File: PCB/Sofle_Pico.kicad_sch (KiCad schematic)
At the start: 83 parts, among them J2 MJ-4PP-9, Q1 Si2301CDS, SW1 SW_PUSH, SW10 SW_PUSH, SW11 SW_PUSH, SW12 SW_PUSH, SW13 SW_PUSH, SW14 SW_PUSH, SW15 SW_PUSH, SW16 SW_PUSH, SW17 SW_PUSH, SW18 SW_PUSH, SW19 SW_PUSH, SW2 SW_PUSH, SW20 SW_PUSH, SW21 SW_PUSH, SW22 SW_PUSH, SW23 SW_PUSH, SW24 SW_PUSH, SW25 SW_PUSH, SW26 SW_PUSH, SW27 SW_PUSH, SW28 SW_PUSH, SW29 SW_PUSH, SW3 SW_PUSH, SW30 SW_PUSH, SW31 SW_PUSH, SW32 SW_PUSH, SW33 SW_PUSH, SW34 SW_PUSH, SW35 SW_PUSH, SW36 SW_PUSH, SW4 SW_PUSH, SW5 SW_PUSH, SW6 SW_PUSH, SW7 SW_PUSH, SW8 SW_PUSH, SW9 SW_PUSH, U2 Pico

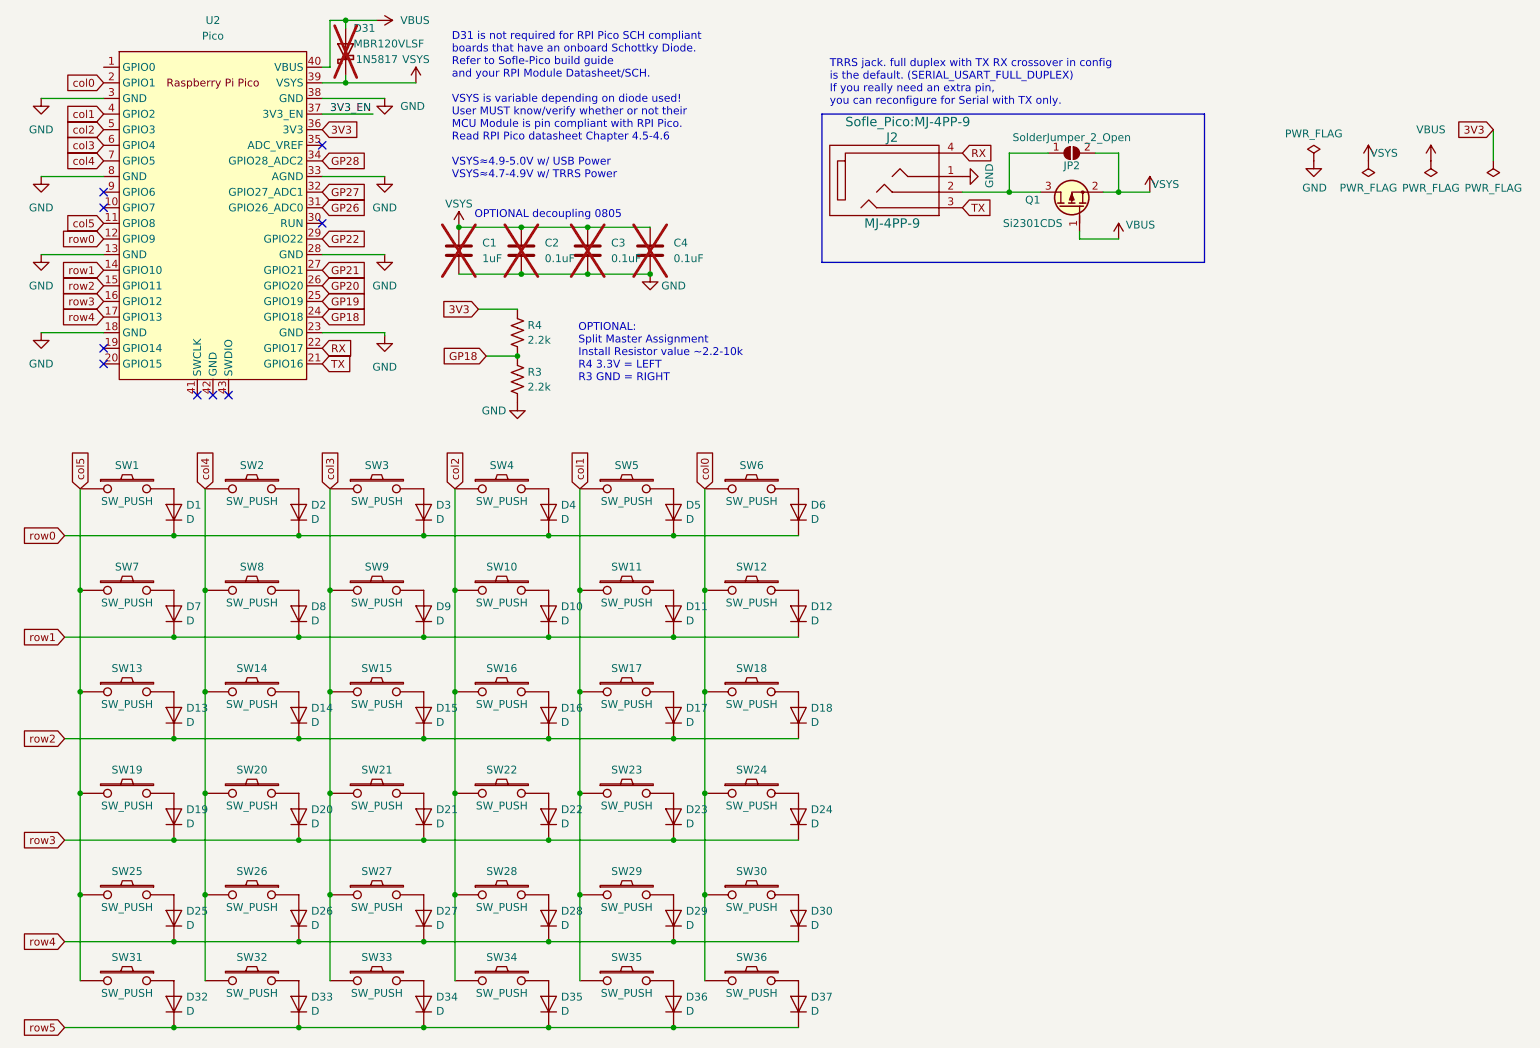
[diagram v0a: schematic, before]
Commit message: second board is not smart
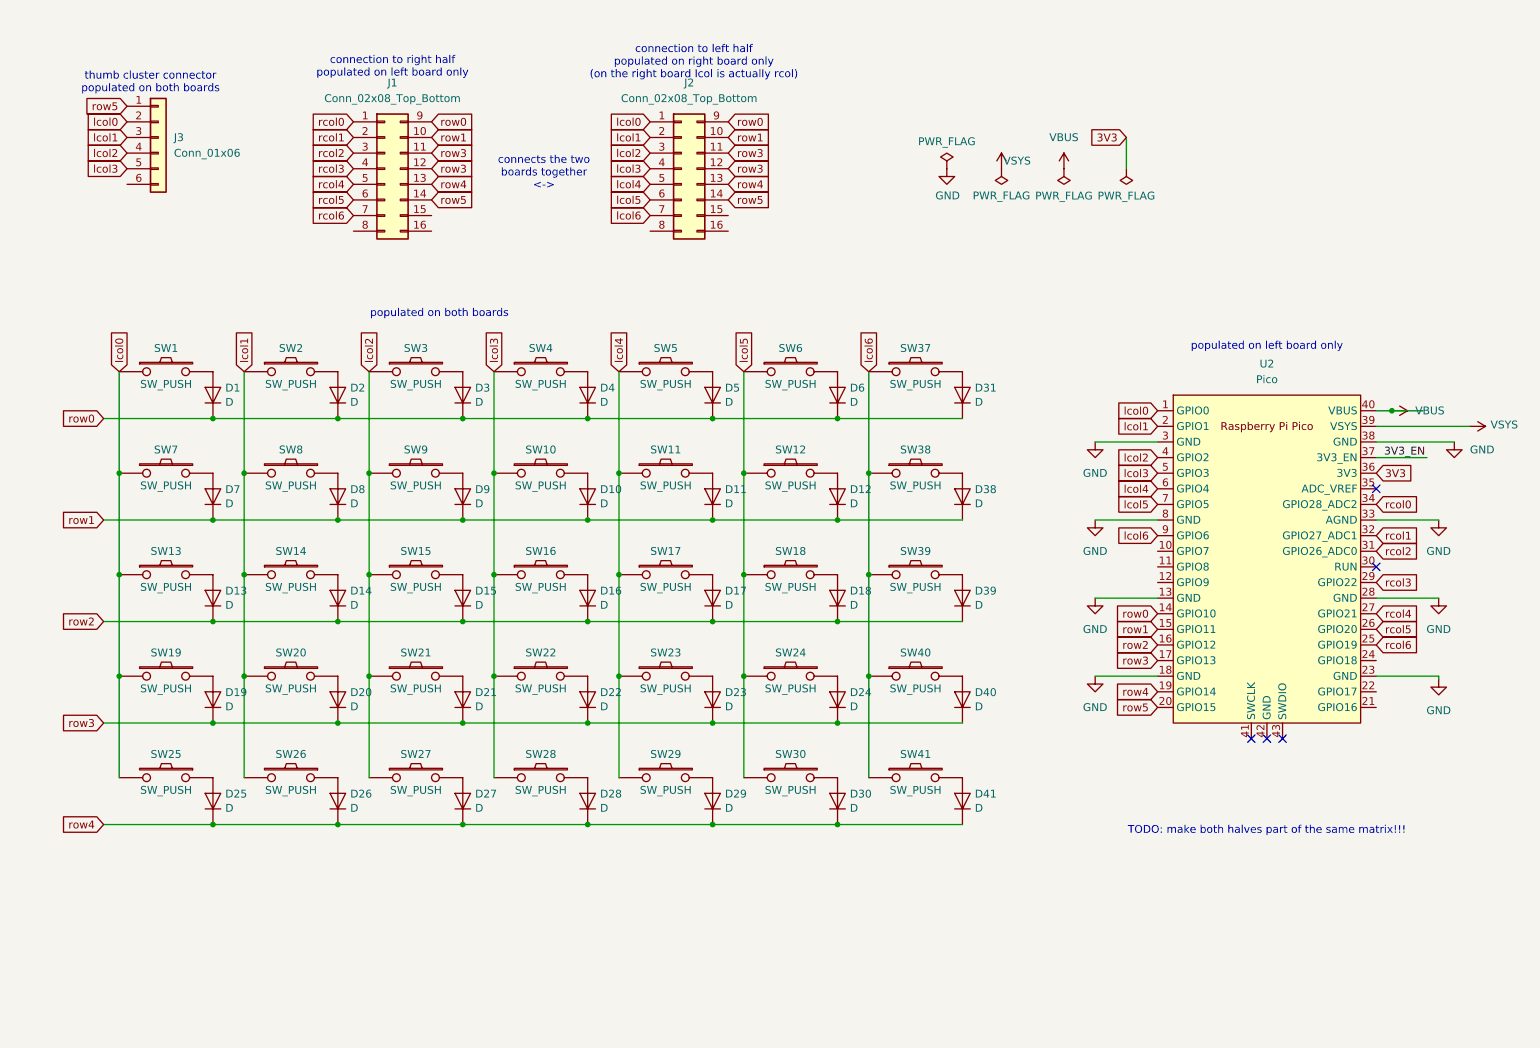
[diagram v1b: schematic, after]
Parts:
- removed C1: 1uF, Capacitor_SMD:C_0805_2012Metric_Pad1.18x1.45mm_HandSolder, symbol Device:C
- removed C2, C3, C4: 0.1uF, Capacitor_SMD:C_0805_2012Metric_Pad1.18x1.45mm_HandSolder, symbol Device:C
- removed D31: MBR120VLSF, Sofle_Pico:D_SOD-123_DO-41_7.62mm_Hybrid_DoubleSided, symbol Diode:1N5817
- removed D32, D33, D34, D35, D36, D37: D, Sofle_Pico:D_SOD-123_DO-35_Hybrid_DoubleSided_V2, symbol SofleKeyboard-rescue:D-Lily58-cache-Lily58_Pro-rescue
- removed J2: MJ-4PP-9, Sofle_Pico:MJ-4PP-9, symbol Sofle_Pico:MJ-4PP-9
- removed JP2: SolderJumper_2_Open, Sofle_Pico:Level Shifter Bypass Jumper, symbol Sofle_Pico:SolderJumper_2_Open
- removed Q1: Si2301CDS, Package_TO_SOT_SMD_AKL:SOT-23, symbol PCM_Transistor_MOSFET_AKL:DMG2305UX
- removed R3, R4: 2.2k, Sofle_Pico:Res_1206_SMD_6.3mm_TH_Hybrid, symbol Device:R_US
- removed SW31, SW32, SW33, SW34, SW35, SW36: SW_PUSH, Sofle_Pico:Cherry_MX_DS_Hotswap_v3.5.4, symbol Sofle_Pico:SW_PUSH
- added D31, D38, D39, D40, D41: D, Sofle_Pico:D_SOD-123_DO-35_Hybrid_DoubleSided_V2, symbol SofleKeyboard-rescue:D-Lily58-cache-Lily58_Pro-rescue
- added J1, J2: Conn_02x08_Top_Bottom, Connector_PinHeader_1.27mm:PinHeader_2x08_P1.27mm_Horizontal, symbol Connector_Generic:Conn_02x08_Top_Bottom
- added J3: Conn_01x06, Connector_PinHeader_1.27mm:PinHeader_1x06_P1.27mm_Horizontal, symbol Connector_Generic:Conn_01x06
- added SW37, SW38, SW39, SW40, SW41: SW_PUSH, Sofle_Pico:Cherry_MX_DS_Hotswap_v3.5.4, symbol Sofle_Pico:SW_PUSH
- U2: footprint Sofle_Pico:RPi_Pico_SMD_TH_DS -> Module:RaspberryPi_Pico_SMD_HandSolder
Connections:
- net row0: now also U2.14 (GPIO10), D31.1 (K), J1.9 (Pin_9), J2.9 (Pin_9); no longer U2.12 (GPIO9)
- net row1: now also U2.15 (GPIO11), D38.1 (K), J1.10 (Pin_10), J2.10 (Pin_10); no longer U2.14 (GPIO10)
- net row2: now also U2.16 (GPIO12), D39.1 (K); no longer U2.15 (GPIO11)
- net row3: now also U2.17 (GPIO13), D40.1 (K), J1.11 (Pin_11), J1.12 (Pin_12), J2.11 (Pin_11), J2.12 (Pin_12); no longer U2.16 (GPIO12)
- net row4: now also U2.19 (GPIO14), D41.1 (K), J1.13 (Pin_13), J2.13 (Pin_13); no longer U2.17 (GPIO13)
- net row5: now also U2.20 (GPIO15), J1.14 (Pin_14), J2.14 (Pin_14), J3.1 (Pin_1)
- net lcol0: now reaches U2.1 (GPIO0)
- net lcol0: now also SW1.1, SW13.1, SW19.1, SW25.2, SW7.1, J2.1 (Pin_1), J3.2 (Pin_2)
- net lcol6: now reaches U2.9 (GPIO6)
- net lcol6: now also J2.7 (Pin_7), SW37.1, SW38.1, SW39.1, SW40.1, SW41.1
- net GP18: no longer names the net of U2.24 (GPIO18)
- net GP19 renamed rcol6
- net rcol6: now also J1.7 (Pin_7)
- net GP20 renamed rcol5
- net rcol5: now also J1.6 (Pin_6)
- net GP21 renamed rcol4
- net rcol4: now also J1.5 (Pin_5)
- net GP22 renamed rcol3
- net rcol3: now also J1.4 (Pin_4)
- net GP26 renamed rcol2
- net rcol2: now also J1.3 (Pin_3)
- net GP27 renamed rcol1
- net rcol1: now also J1.2 (Pin_2)
- net GP28 renamed rcol0
- net rcol0: now also J1.1 (Pin_1)
- net RX: no longer names the net of U2.22 (GPIO17)
- net TX: no longer names the net of U2.21 (GPIO16)
- net col0 renamed lcol5
- net lcol5: now also U2.7 (GPIO5), J2.6 (Pin_6); no longer U2.2 (GPIO1)
- net col1 renamed lcol4
- net lcol4: now also U2.6 (GPIO4), J2.5 (Pin_5); no longer U2.4 (GPIO2)
- net col2 renamed lcol3
- net lcol3: now also J2.4 (Pin_4), J3.5 (Pin_5)
- net col3 renamed lcol2
- net lcol2: now also U2.4 (GPIO2), J2.3 (Pin_3), J3.4 (Pin_4); no longer U2.6 (GPIO4)
- net col4 renamed lcol1
- net lcol1: now also U2.2 (GPIO1), J2.2 (Pin_2), J3.3 (Pin_3); no longer U2.7 (GPIO5)
- removed net col5: SW1.1, SW13.1, SW19.1, SW25.2, SW7.1, U2.11 (GPIO8)
- new net: D41.2 (A), SW41.2
- new net: D31.2 (A), SW37.2
- new net: D40.2 (A), SW40.2
- new net: D39.2 (A), SW39.2
- new net: D38.2 (A), SW38.2
- no-connect marks 9 -> 5
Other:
- note added: "TODO: make both halves part of the same matrix!!!"
- note added: "connection to left half populated on right board only (on the right board lcol is actually rcol)"
- note added: "connection to right half populated on left board only"
- note added: "connects the two boards together <->"
- note added: "populated on both boards"
- note added: "populated on left board only"
- note added: "thumb cluster connector populated on both boards"
- note removed: "D31 is not required for RPI Pico SCH compliant boards that have an onboard Schottky Diode. Refer to Sofle-Pico build guide and your RPI Module Datasheet/SCH. VSYS is variable depending on diode used! User MUST know/verify whether or not their MCU Module is pin compliant with RPI Pico. Read RPI Pico datasheet Chapter 4.5-4.6 VSYS≈4.9-5.0V w/ USB Power VSYS≈4.7-4.9V w/ TRRS Power"
- note removed: "OPTIONAL decoupling 0805"
- note removed: "OPTIONAL: Split Master Assignment Install Resistor value ~2.2-10k R4 3.3V = LEFT R3 GND = RIGHT"
- note removed: "TRRS jack. full duplex with TX RX crossover in config is the default. (SERIAL_USART_FULL_DUPLEX) If you really need an extra pin, you can reconfigure for Serial with TX only."
- moved on the sheet: D1, D10, D11, D12, D13, D14, D15, D16, D17, D18, D19, D2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

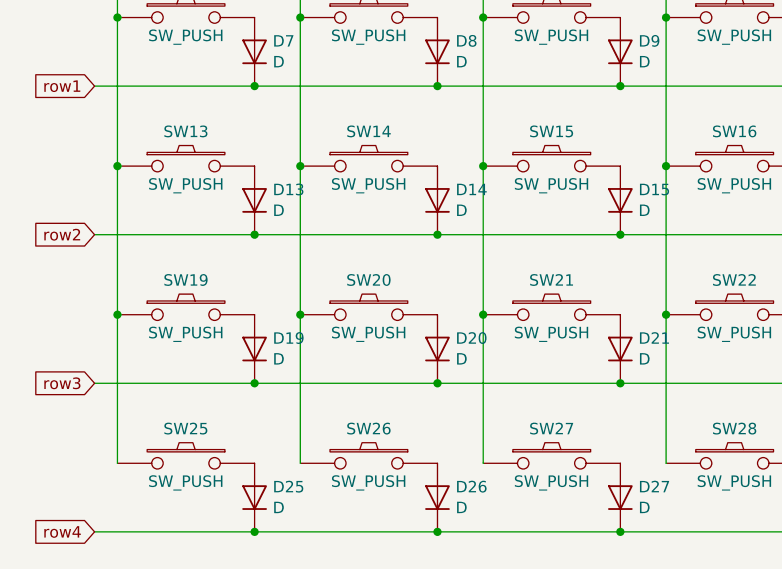
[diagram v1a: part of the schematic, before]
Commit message: chop off unneeded keys
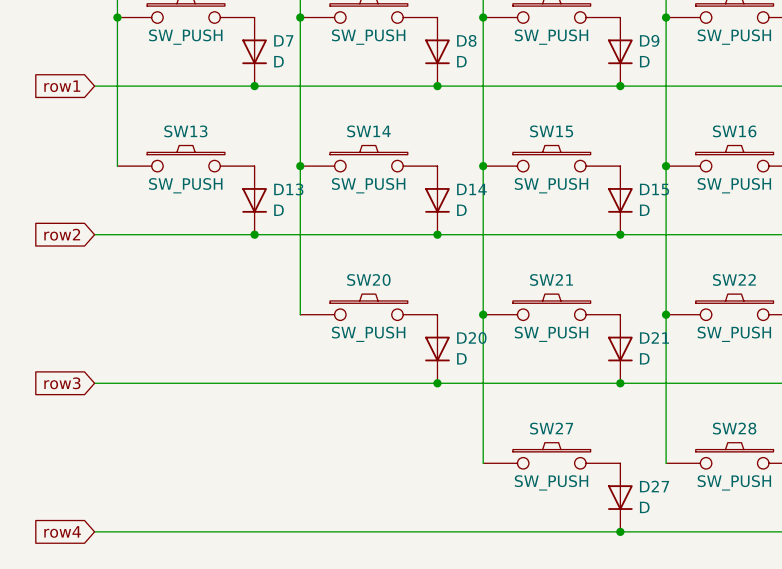
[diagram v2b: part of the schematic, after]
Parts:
- removed D19, D25, D26: D, Sofle_Pico:D_SOD-123_DO-35_Hybrid_DoubleSided_V2, symbol SofleKeyboard-rescue:D-Lily58-cache-Lily58_Pro-rescue
- removed SW19, SW25, SW26: SW_PUSH, Sofle_Pico:Cherry_MX_DS_Hotswap_v3.5.4, symbol Sofle_Pico:SW_PUSH
